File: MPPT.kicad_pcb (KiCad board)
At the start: 2 copper layers, 172.7 x 116.8 mm, 127 parts, among them J1 Solar Array, J2 Battery, J3 Car Power, J4 CAN_In, J5 CAN_Out, Q1 NMOS, Q2 NMOS, SW1 RESET, SW2 CAN Address, U1 PQMC3-D12-S9-S, U2 Nucleo_L432KC, U3 UCC37321, U4 INA210, U5 ADM3055E, U6 INA210, U7 CDSOT23-T24CAN, U8 MAX400_option2, U9 MAX400_option2

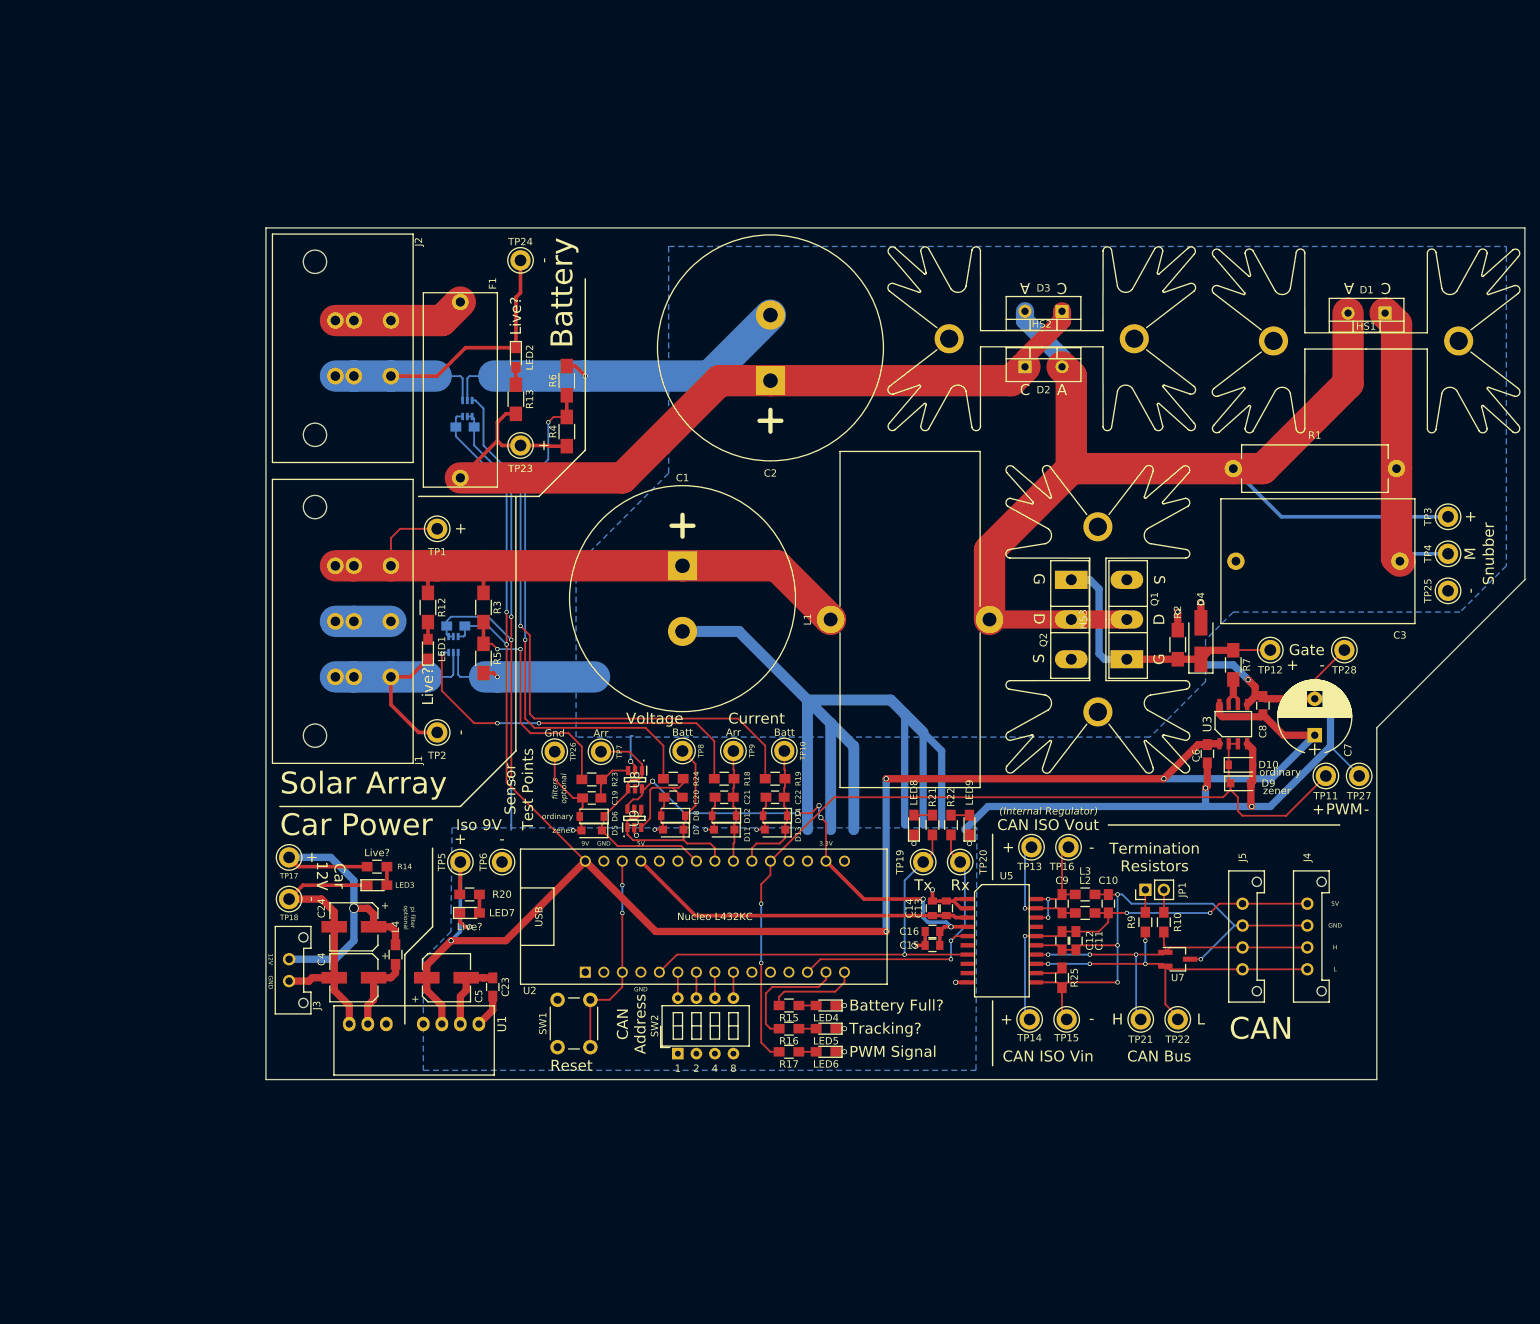
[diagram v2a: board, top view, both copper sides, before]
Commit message: Major MPPT Board update. Overhaul of layout, and cleanup of the schematic. Added further documentation and updated instructions in the README. Added unity gain op amp for voltage sensors.
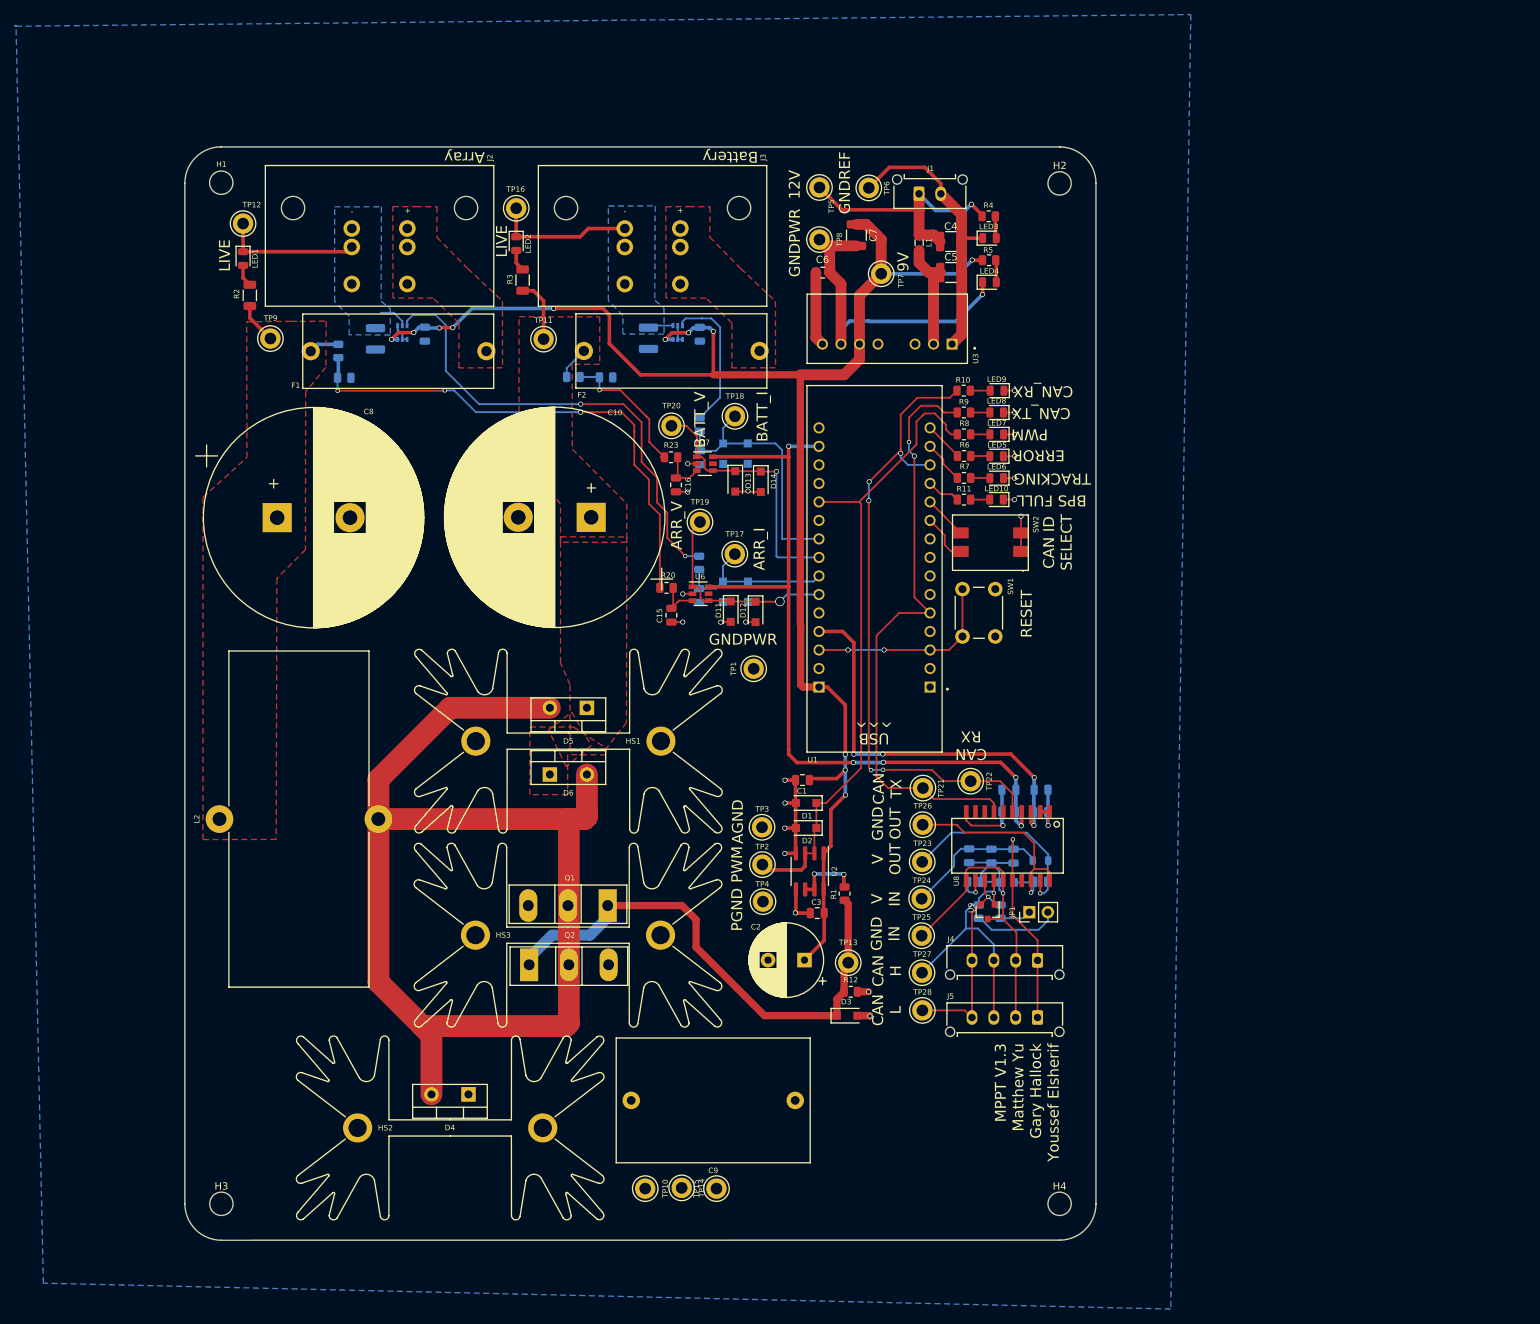
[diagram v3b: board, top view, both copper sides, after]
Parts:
- removed R13: 40K, Resistors_SMD:R_1206_HandSoldering
- added F2: Fuse, MPPT-PrimaryPCB:05200101Z_Fuze_Holder_5x20_PCB_Mount, F.Cu at (99.8, 53.1)
- added H1: Top Left Mounting Hole, MountingHole:MountingHole_3.2mm_M3, F.Cu at (25.0, 25.0)
- added H2: Top Right Mounting Hole, MountingHole:MountingHole_3.2mm_M3, F.Cu at (140.0, 25.0)
- added H3: Bottom Left Mounting Hole, MountingHole:MountingHole_3.2mm_M3, F.Cu at (25.0, 165.0)
- added H4: Bottom Right Mounting Hole, MountingHole:MountingHole_3.2mm_M3, F.Cu at (140.0, 165.0)
- added LED10: BPS Full (Blue), LED_SMD:LED_0805_2012Metric, F.Cu at (131.3, 68.4)
- added R26: 60, Resistor_SMD:R_0805_2012Metric, B.Cu at (131.9, 124.9)
- C1: value 1000uF -> 0.1uF; footprint UTSVT_Passive:CP_Radial_D31mm_P9mm -> Capacitor_SMD:C_0805_2012Metric
- C10: value 0.22u -> 1000uF; footprint Capacitors_SMD:C_0805_HandSoldering -> Capacitor_THT:CP_Radial_D30.0mm_P10.00mm_SnapIn
- C11: value 0.1u -> 0.1uF; footprint Capacitors_SMD:C_0805_HandSoldering -> Capacitor_SMD:C_0805_2012Metric; moved to B.Cu
- C12: value 0.01u -> 1uF; footprint Capacitors_SMD:C_0805_HandSoldering -> Capacitor_SMD:C_0805_2012Metric; moved to B.Cu
- C13: value 10u -> 0.1uF; footprint Capacitors_SMD:C_0805 -> Capacitor_SMD:C_0805_2012Metric; moved to B.Cu
- C14: value 0.1u -> 1uF; footprint Capacitors_SMD:C_0805 -> Capacitor_SMD:C_0805_2012Metric; moved to B.Cu
- C15: value 0.1u -> 1uF; footprint Capacitors_SMD:C_0805 -> Capacitor_SMD:C_0805_2012Metric
- C16: value 0.01u -> 1uF; footprint Capacitors_SMD:C_0805 -> Capacitor_SMD:C_0805_2012Metric
- C17: value 0.1uF -> 10uF; footprint Capacitors_SMD:C_0805_HandSoldering -> Capacitor_SMD:C_0805_2012Metric
- C18: footprint Capacitors_SMD:C_0805_HandSoldering -> Capacitor_SMD:C_0805_2012Metric
- C19: value 1uF -> 0.1uF; footprint Capacitors_SMD:C_0805_HandSoldering -> Capacitor_SMD:C_0805_2012Metric; moved to B.Cu
- C2: value 1000uF -> 1uF; footprint UTSVT_Passive:CP_Radial_D31mm_P9mm -> Capacitor_THT:CP_Radial_D10.0mm_P5.00mm
- C20: value 1uF -> 0.01uF; footprint Capacitors_SMD:C_0805_HandSoldering -> Capacitor_SMD:C_0805_2012Metric; moved to B.Cu
- C21: value 1uF -> 0.22uF; footprint Capacitors_SMD:C_0805_HandSoldering -> Capacitor_SMD:C_0805_2012Metric; moved to B.Cu
- C22: value 1uF -> 10uF; footprint Capacitors_SMD:C_0805_HandSoldering -> Capacitor_SMD:C_0805_2012Metric; moved to B.Cu
- C23: value 10u -> 0.01uF; footprint Capacitors_SMD:C_0805_HandSoldering -> Capacitor_SMD:C_0805_2012Metric; moved to B.Cu
- C24: value 100u -> 0.1uF; footprint Capacitors_SMD:CP_Elec_6.3x7.7 -> Capacitor_SMD:C_0805_2012Metric; moved to B.Cu
- C3: value CP -> 0.1uF; footprint MPPT_Custom:C_Rect_L26.5mm_W17.0mm_P22.50mm_MKS4 -> Capacitor_SMD:C_0805_2012Metric
- C4: value 47u -> 100uF; footprint Capacitors_SMD:CP_Elec_6.3x5.3 -> Capacitor_SMD:C_1210_3225Metric
- C5: value 100u -> 47uF; footprint Capacitors_SMD:CP_Elec_6.3x7.7 -> Capacitor_SMD:C_1210_3225Metric
- C6: value 0.1u -> 10uF; footprint Capacitors_SMD:C_0805_HandSoldering -> Capacitor_SMD:C_0805_2012Metric
- C7: value 1u -> 100uF; footprint Capacitors_THT:CP_Radial_D10.0mm_P5.00mm -> Capacitor_SMD:C_1210_3225Metric
- C8: value 0.1u -> 1000uF; footprint Capacitors_SMD:C_0805_HandSoldering -> Capacitor_THT:CP_Radial_D30.0mm_P10.00mm_SnapIn
- C9: value 10u -> CP; footprint Capacitors_SMD:C_0805_HandSoldering -> MPPT_Custom:C_Rect_L26.5mm_W17.0mm_P22.50mm_MKS4
- D1: value Schottky -> 3.9V Zener; footprint TO_SOT_Packages_THT:TO-220-2_Vertical -> Diode_SMD:D_SOD-123F
- D10, D8: footprint Diodes_SMD:D_SOD-123 -> Diode_SMD:D_SOD-123F; moved to B.Cu
- D11, D13: value 4V Zener -> 3.9V Zener; footprint Diodes_SMD:D_SOD-123F -> Diode_SMD:D_SOD-123F
- D12, D14: footprint Diodes_SMD:D_SOD-123 -> Diode_SMD:D_SOD-123F
- D2: value Schottky -> Diode; footprint TO_SOT_Packages_THT:TO-220-2_Vertical -> Diode_SMD:D_SOD-123F
- D3: value Schottky -> 16.3V Zener; footprint TO_SOT_Packages_THT:TO-220-2_Vertical -> Diode_SMD:D_SOD-123F
- D4: value 18V Zener -> Schottky; footprint Diodes_SMD:D_SMA_Handsoldering -> Package_TO_SOT_THT:TO-220-2_Vertical
- D5: value 4V Zener -> Schottky; footprint Diodes_SMD:D_SOD-123F -> Package_TO_SOT_THT:TO-220-2_Vertical
- D6: value Diode -> Schottky; footprint Diodes_SMD:D_SOD-123 -> Package_TO_SOT_THT:TO-220-2_Vertical
- D7, D9: value 4V Zener -> 3.9V Zener; footprint Diodes_SMD:D_SOD-123F -> Diode_SMD:D_SOD-123F; moved to B.Cu
- F1: footprint UTSVT_Passive:LittelFuse_OMNIBLOK_520Series_PCB -> MPPT-PrimaryPCB:05200101Z_Fuze_Holder_5x20_PCB_Mount
- HS1: value Heatsink -> Schottky Diode Heatsink
- HS2: value Heatsink -> Snubber Heatsink
- HS3: value Heatsink -> MOSFET Heatsink
- J1: value Solar Array -> Car Power; footprint UTSVT_Connectors:PhoenixContact_PowerCombicon5_GF_3x7.62mm -> Connector_Molex:Molex_Micro-Fit_3.0_43650-0215_1x02_P3.00mm_Vertical
- J2: value Battery -> Solar Array; footprint UTSVT_Connectors:PhoenixContact_PowerCombicon5_GF_2x7.62mm -> MPPT-PrimaryPCB:PhoenixContact_PowerCombicon5_GF_2x7.62mm
- J3: value Car Power -> Battery; footprint UTSVT_Connectors:Molex_MicroFit3.0_1x2xP3.00mm_PolarizingPeg_Vertical -> MPPT-PrimaryPCB:PhoenixContact_PowerCombicon5_GF_2x7.62mm
- J4, J5: footprint UTSVT_Connectors:Molex_MicroFit3.0_1x4xP3.00mm_PolarizingPeg_Vertical -> Connector_Molex:Molex_Micro-Fit_3.0_43650-0415_1x04_P3.00mm_Vertical
- JP1: footprint Pin_Headers:Pin_Header_Straight_1x02_Pitch2.54mm -> Connector_PinHeader_2.54mm:PinHeader_1x02_P2.54mm_Vertical
- L1: value 560uH -> 4.7uH; footprint Inductors_THT:L_Toroid_Vertical_L46.0mm_W19.1mm_P21.80mm_Bourns_5700 -> Inductor_SMD:L_0805_2012Metric
- L2: value 2k -> 560uH; footprint Inductors_SMD:L_0805_HandSoldering -> MPPT-PrimaryPCB:L_Toroid_Vertical_L46.0mm_W19.1mm_P21.80mm_Bourns_5700
- L3: value 2k -> 1.8kH; footprint Inductors_SMD:L_0805_HandSoldering -> Inductor_SMD:L_0805_2012Metric; moved to B.Cu
- L4: value 4.7u -> 1.8kH; footprint Inductors_SMD:L_0805_HandSoldering -> Inductor_SMD:L_0805_2012Metric; moved to B.Cu
- LED1: value Array Live? -> Array Live (Green); footprint LEDs:LED_0805_HandSoldering -> LED_SMD:LED_0805_2012Metric
- LED2: value Battery Live? -> Battery Live (Green); footprint LEDs:LED_0805_HandSoldering -> LED_SMD:LED_0805_2012Metric
- LED3: value Car Power Live? -> Car Power Live (Green); footprint LEDs:LED_0805_HandSoldering -> LED_SMD:LED_0805_2012Metric
- LED4: value Battery Full? -> Device 9V Live (Green); footprint LEDs:LED_0805_HandSoldering -> LED_SMD:LED_0805_2012Metric
- LED5: value Tracking? -> Error (Amber); footprint LEDs:LED_0805_HandSoldering -> LED_SMD:LED_0805_2012Metric
- LED6: value PWM -> Tracking (Blue); footprint LEDs:LED_0805_HandSoldering -> LED_SMD:LED_0805_2012Metric
- LED7: value Iso 9V Live? -> PWM (Blue); footprint LEDs:LED_0805_HandSoldering -> LED_SMD:LED_0805_2012Metric
- LED8: value CAN_Tx -> CAN_Tx (Blue); footprint LEDs:LED_0805_HandSoldering -> LED_SMD:LED_0805_2012Metric
- LED9: value CAN_Rx -> CAN_Rx (Blue); footprint LEDs:LED_0805_HandSoldering -> LED_SMD:LED_0805_2012Metric
- Q1, Q2: footprint TO_SOT_Packages_THT:TO-247_TO-3P_Vertical -> Package_TO_SOT_THT:TO-247-3_Vertical
- R1: value R -> 1.5; footprint Resistors_THT:R_Axial_Power_L20.0mm_W6.4mm_P22.40mm -> Resistor_SMD:R_0805_2012Metric
- R10, R9: value 60 -> 330; footprint Resistors_SMD:R_0805_HandSoldering -> Resistor_SMD:R_0805_2012Metric
- R11, R8: value 2m -> 330; footprint Resistors_SMD:R_2512_HandSoldering -> Resistor_SMD:R_0805_2012Metric; moved to F.Cu
- R12: value 40K -> 10k; footprint Resistors_SMD:R_1206_HandSoldering -> Resistor_SMD:R_0805_2012Metric
- R14: value 2K -> 2m; footprint Resistors_SMD:R_0805_HandSoldering -> Resistor_SMD:R_1210_3225Metric; moved to B.Cu
- R15, R17: value 330R -> 1.7k; footprint Resistors_SMD:R_0805_HandSoldering -> Resistor_SMD:R_0805_2012Metric; moved to B.Cu
- R16: value 330R -> 2m; footprint Resistors_SMD:R_0805_HandSoldering -> Resistor_SMD:R_1210_3225Metric; moved to B.Cu
- R18: value 1.7k -> 100k; footprint Resistors_SMD:R_0805_HandSoldering -> Resistor_SMD:R_0805_2012Metric; moved to B.Cu
- R19: value 1.7k -> 2k; footprint Resistors_SMD:R_0805_HandSoldering -> Resistor_SMD:R_0805_2012Metric; moved to B.Cu
- R2: value 10k -> 15k; footprint Resistors_SMD:R_1206_HandSoldering -> Resistor_SMD:R_1206_3216Metric
- R20: value 1K -> 1.7k; footprint Resistors_SMD:R_0805_HandSoldering -> Resistor_SMD:R_0805_2012Metric
- R21: value 330R -> 100k; footprint Resistors_SMD:R_0805_HandSoldering -> Resistor_SMD:R_0805_2012Metric; moved to B.Cu
- R22: value 330R -> 2k; footprint Resistors_SMD:R_0805_HandSoldering -> Resistor_SMD:R_0805_2012Metric; moved to B.Cu
- R23: footprint Resistors_SMD:R_0805_HandSoldering -> Resistor_SMD:R_0805_2012Metric
- R24: value 1.7k -> 0; footprint Resistors_SMD:R_0805_HandSoldering -> Resistor_SMD:R_0805_2012Metric; moved to B.Cu
- R25: value 0 -> 60; footprint Resistors_SMD:R_0805_HandSoldering -> Resistor_SMD:R_0805_2012Metric; moved to B.Cu
- R3: value 100k -> 27k; footprint Resistors_SMD:R_1206_HandSoldering -> Resistor_SMD:R_1206_3216Metric
- R4: value 100k -> 1.5k; footprint Resistors_SMD:R_1206_HandSoldering -> Resistor_SMD:R_0805_2012Metric
- R5: value 2k -> 1.1k; footprint Resistors_SMD:R_1206_HandSoldering -> Resistor_SMD:R_0805_2012Metric
- R6: value 2k -> 330; footprint Resistors_SMD:R_1206_HandSoldering -> Resistor_SMD:R_0805_2012Metric
- R7: value 1R5 -> 330; footprint Resistors_SMD:R_1206_HandSoldering -> Resistor_SMD:R_0805_2012Metric
- SW1: footprint Buttons_Switches_THT:SW_PUSH_6mm -> Button_Switch_THT:SW_PUSH_6mm
- SW2: value CAN Address -> SW_DIP_x02; footprint Buttons_Switches_THT:SW_DIP_x4_W7.62mm_Slide_LowProfile -> MPPT-PrimaryPCB:ADF02ST04_DIP_Switch_2_POS
- TP1: value +ARR -> GND; footprint Measurement_Points:Test_Point_Keystone_5005-5009_Compact -> TestPoint:TestPoint_Keystone_5005-5009_Compact
- TP10: value Batt_I -> +SNUB; footprint Measurement_Points:Test_Point_Keystone_5005-5009_Compact -> TestPoint:TestPoint_Keystone_5005-5009_Compact
- TP11: value PWM -> +BATT; footprint Measurement_Points:Test_Point_Keystone_5005-5009_Compact -> TestPoint:TestPoint_Keystone_5005-5009_Compact
- TP12: value GATE -> -ARR; footprint Measurement_Points:Test_Point_Keystone_5005-5009_Compact -> TestPoint:TestPoint_Keystone_5005-5009_Compact
- TP13: value CAN_ISO_Vout -> GATE; footprint Measurement_Points:Test_Point_Keystone_5005-5009_Compact -> TestPoint:TestPoint_Keystone_5005-5009_Compact
- TP14: value CAN_ISO_Vin -> M_SNUB; footprint Measurement_Points:Test_Point_Keystone_5005-5009_Compact -> TestPoint:TestPoint_Keystone_5005-5009_Compact
- TP15: value CAN_ISO_GndIn -> -SNUB; footprint Measurement_Points:Test_Point_Keystone_5005-5009_Compact -> TestPoint:TestPoint_Keystone_5005-5009_Compact
- TP16: value CAN_ISO_GndOut -> -BATT; footprint Measurement_Points:Test_Point_Keystone_5005-5009_Compact -> TestPoint:TestPoint_Keystone_5005-5009_Compact
- TP17: value Car +12V -> Arr_I; footprint Measurement_Points:Test_Point_Keystone_5005-5009_Compact -> TestPoint:TestPoint_Keystone_5005-5009_Compact
- TP18: value Car GND -> Batt_I; footprint Measurement_Points:Test_Point_Keystone_5005-5009_Compact -> TestPoint:TestPoint_Keystone_5005-5009_Compact
- TP19: value CAN_Tx -> Arr_V; footprint Measurement_Points:Test_Point_Keystone_5005-5009_Compact -> TestPoint:TestPoint_Keystone_5005-5009_Compact
- TP2: value -ARR -> PWM; footprint Measurement_Points:Test_Point_Keystone_5005-5009_Compact -> TestPoint:TestPoint_Keystone_5005-5009_Compact
- TP20: value CAN_Rx -> Batt_V; footprint Measurement_Points:Test_Point_Keystone_5005-5009_Compact -> TestPoint:TestPoint_Keystone_5005-5009_Compact
- TP21: value CAN_H -> CAN_Tx; footprint Measurement_Points:Test_Point_Keystone_5005-5009_Compact -> TestPoint:TestPoint_Keystone_5005-5009_Compact
- TP22: value CAN_L -> CAN_Rx; footprint Measurement_Points:Test_Point_Keystone_5005-5009_Compact -> TestPoint:TestPoint_Keystone_5005-5009_Compact
- TP23: value +BATT -> CAN_ISO_Vout; footprint Measurement_Points:Test_Point_Keystone_5005-5009_Compact -> TestPoint:TestPoint_Keystone_5005-5009_Compact
- TP24: value -BATT -> CAN_ISO_Vin; footprint Measurement_Points:Test_Point_Keystone_5005-5009_Compact -> TestPoint:TestPoint_Keystone_5005-5009_Compact
- TP25: value -SNUB -> CAN_ISO_GndIn; footprint Measurement_Points:Test_Point_Keystone_5005-5009_Compact -> TestPoint:TestPoint_Keystone_5005-5009_Compact
- TP26: value GND -> CAN_ISO_GndOut; footprint Measurement_Points:Test_Point_Keystone_5005-5009_Compact -> TestPoint:TestPoint_Keystone_5005-5009_Compact
- TP27: value AGND -> CAN_H; footprint Measurement_Points:Test_Point_Keystone_5005-5009_Compact -> TestPoint:TestPoint_Keystone_5005-5009_Compact
- TP28: value PGND -> CAN_L; footprint Measurement_Points:Test_Point_Keystone_5005-5009_Compact -> TestPoint:TestPoint_Keystone_5005-5009_Compact
- TP3: value +SNUB -> AGND; footprint Measurement_Points:Test_Point_Keystone_5005-5009_Compact -> TestPoint:TestPoint_Keystone_5005-5009_Compact
- TP4: value M_SNUB -> PGND; footprint Measurement_Points:Test_Point_Keystone_5005-5009_Compact -> TestPoint:TestPoint_Keystone_5005-5009_Compact
- TP5: value +9VA -> Car +12V; footprint Measurement_Points:Test_Point_Keystone_5005-5009_Compact -> TestPoint:TestPoint_Keystone_5005-5009_Compact
- TP6: value GNDP -> Car GND; footprint Measurement_Points:Test_Point_Keystone_5005-5009_Compact -> TestPoint:TestPoint_Keystone_5005-5009_Compact
- TP7: value Arr_V -> +9VA; footprint Measurement_Points:Test_Point_Keystone_5005-5009_Compact -> TestPoint:TestPoint_Keystone_5005-5009_Compact
- TP8: value Batt_V -> GNDP; footprint Measurement_Points:Test_Point_Keystone_5005-5009_Compact -> TestPoint:TestPoint_Keystone_5005-5009_Compact
- TP9: value Arr_I -> +ARR; footprint Measurement_Points:Test_Point_Keystone_5005-5009_Compact -> TestPoint:TestPoint_Keystone_5005-5009_Compact
- U1: value PQMC3-D12-S9-S -> Nucleo_L432KC; footprint UTSVT_ICs:CUI_PQMC3-S -> MPPT-PrimaryPCB:MODULE_NUCLEO-L432KC
- U2: value Nucleo_L432KC -> UCC37321; footprint UTSVT_Special:NucleoL432KC -> Package_SO:SOIC-8_3.9x4.9mm_P1.27mm
- U3: value UCC37321 -> PQMC3-D12-S9-S; footprint UTSVT_ICs:SOIC-8_4.00x5.00mm_Pitch1.27mm -> MPPT-PrimaryPCB:490_PQMC3_D12_S12_S
- U4: footprint UTSVT_ICs:SOIC-6_1.40x2.15mm_Pitch0.65mm -> MPPT-PrimaryPCB:SC70-6
- U5: value ADM3055E -> INA210; footprint UTSVT_ICs:SOIC-20W_7.5x15.4mm_Pitch1.27mm -> MPPT-PrimaryPCB:SC70-6; moved to B.Cu
- U6: value INA210 -> MAX40075AUT+; footprint UTSVT_ICs:SOIC-6_1.40x2.15mm_Pitch0.65mm -> Package_TO_SOT_SMD:SOT-23-6; moved to F.Cu
- U7: value CDSOT23-T24CAN -> MAX40075AUT+; footprint TO_SOT_Packages_SMD:SOT-23W_Handsoldering -> Package_TO_SOT_SMD:SOT-23-6
- U8: value MAX400_option2 -> ADM3055E; footprint MPPT_Custom:SOT95P280X145-6N -> MPPT-PrimaryPCB:ADM3055EBRIZ
- U9: value MAX400_option2 -> CDSOT23-T24CAN; footprint MPPT_Custom:SOT95P280X145-6N -> Package_TO_SOT_SMD:SOT-23
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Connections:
- C1 pad 1: /+Arr -> GNDPWR
- C1 pad 2: GNDPWR -> +9VA
- C10 pad 1: Net-(C10-Pad1) -> /+Batt
- C10 pad 2: Net-(C10-Pad2) -> GNDPWR
- C11 pad 1: Net-(C10-Pad1) -> +9VA
- C11 pad 2: Net-(C10-Pad2) -> GNDPWR
- C12 pad 1: Net-(C10-Pad1) -> /Array_Current
- C12 pad 2: Net-(C10-Pad2) -> GNDPWR
- C13 pad 1: +5V -> +9VA
- C14 pad 1: +5V -> /Battery_Current
- C15 pad 1: +3V3 -> Net-(C15-Pad1)
- C16 pad 1: +3V3 -> Net-(C16-Pad1)
- C17 pad 1: +9VA -> +5V
- C18 pad 1: +9VA -> +5V
- C19 pad 1: Net-(C19-Pad1) -> +3V3
- C2 pad 1: /+Batt -> +9VA
- C20 pad 1: Net-(C20-Pad1) -> +3V3
- C21 pad 1: /Array_Current -> Net-(C21-Pad1)
- C21 pad 2: GNDPWR -> Net-(C21-Pad2)
- C22 pad 1: /Battery_Current -> Net-(C22-Pad1)
- C22 pad 2: GNDPWR -> Net-(C22-Pad2)
- C23 pad 1: GNDPWR -> Net-(C22-Pad1)
- C23 pad 2: Net-(C23-Pad2) -> Net-(C22-Pad2)
- C24 pad 1: +12V -> Net-(C22-Pad1)
- C24 pad 2: GNDREF -> Net-(C22-Pad2)
- C3 pad 1: Net-(C3-Pad1) -> +9VA
- C4 pad 1: Net-(C4-Pad1) -> +12V
- C5 pad 1: +9VA -> Net-(C5-Pad1)
- C5 pad 2: GNDPWR -> GNDREF
- C6 pad 2: +9VA -> Net-(C6-Pad2)
- C8 pad 1: +9VA -> /+Arr
- C9 pad 2: Net-(C9-Pad2) -> GNDPWR
- D1 pad 1: Net-(C3-Pad1) -> /PWM
- D1 pad 2: Net-(D1-Pad2) -> GNDPWR
- D10 pad 1: /PWM -> /Battery_Current
- D11 pad 1: /Array_Current -> /Array_Voltage
- D12 pad 1: /Array_Current -> /Array_Voltage
- D13 pad 1: /Battery_Current -> /Battery_Voltage
- D14 pad 1: /Battery_Current -> /Battery_Voltage
- D2 pad 1: /+Batt -> /PWM
- D2 pad 2: Net-(D1-Pad2) -> GNDPWR
- D3 pad 1: /+Batt -> /Drive_PWM
- D3 pad 2: Net-(D1-Pad2) -> GNDPWR
- D4 pad 1: /Drive_PWM -> Net-(C9-Pad1)
- D4 pad 2: GNDPWR -> Net-(D4-Pad2)
- D5 pad 1: /Array_Voltage -> /+Batt
- D5 pad 2: GNDPWR -> Net-(D4-Pad2)
- D6 pad 1: /Array_Voltage -> /+Batt
- D6 pad 2: GNDPWR -> Net-(D4-Pad2)
- D7 pad 1: /Battery_Voltage -> /Array_Current
- D8 pad 1: /Battery_Voltage -> /Array_Current
- D9 pad 1: /PWM -> /Battery_Current
- F1 pad 2: /+Batt -> /+Arr
- J1 pad 1: /+Arr -> +12V
- J1 pad 2: Net-(J1-Pad2) -> GNDREF
- J2 pad 2: /-Batt -> /-Arr
- J3 pad 1: +12V -> Net-(F2-Pad1)
- J3 pad 2: GNDREF -> /-Batt
- J4 pad 1: Net-(C10-Pad1) -> Net-(C22-Pad1)
- J4 pad 2: Net-(C10-Pad2) -> Net-(C22-Pad2)
- J5 pad 1: Net-(C10-Pad1) -> Net-(C22-Pad1)
- J5 pad 2: Net-(C10-Pad2) -> Net-(C22-Pad2)
- L1 pad 1: /+Arr -> +12V
- L1 pad 2: Net-(D1-Pad2) -> Net-(C5-Pad1)
- L2 pad 1: Net-(C10-Pad1) -> /+Arr
- L2 pad 2: Net-(C9-Pad1) -> Net-(D4-Pad2)
- L3 pad 1: Net-(C10-Pad2) -> Net-(C22-Pad1)
- L3 pad 2: Net-(C9-Pad2) -> Net-(C21-Pad1)
- L4 pad 1: +12V -> Net-(C22-Pad2)
- L4 pad 2: Net-(C4-Pad1) -> Net-(C21-Pad2)
- Q1 pad 2: Net-(D1-Pad2) -> Net-(D4-Pad2)
- Q2 pad 2: Net-(D1-Pad2) -> Net-(D4-Pad2)
- R1 pad 1: Net-(D1-Pad2) -> /Drive_PWM
- R1 pad 2: Net-(C3-Pad1) -> Net-(R1-Pad2)
- R10 pad 1: Net-(JP1-Pad2) -> Net-(LED9-Pad2)
- R10 pad 2: Net-(J4-Pad3) -> /CAN_Rx
- R11 pad 1: /-Batt -> Net-(LED10-Pad2)
- R11 pad 2: GNDPWR -> /BPS_Full
- R12 pad 1: Net-(LED1-Pad2) -> /Drive_PWM
- R12 pad 2: /+Arr -> GNDPWR
- R14 pad 1: Net-(LED3-Pad2) -> GNDPWR
- R14 pad 2: +12V -> /-Arr
- R15 pad 1: Net-(LED4-Pad2) -> Net-(R15-Pad1)
- R15 pad 2: /Battery_Full -> /Array_Current
- R16 pad 1: Net-(LED5-Pad2) -> /-Batt
- R16 pad 2: /Tracking -> GNDPWR
- R17 pad 1: Net-(LED6-Pad2) -> Net-(R17-Pad1)
- R17 pad 2: /PWM -> /Battery_Current
- R18 pad 1: Net-(R18-Pad1) -> /+Arr
- R18 pad 2: /Array_Current -> Net-(R18-Pad2)
- R19 pad 1: Net-(R19-Pad1) -> Net-(R18-Pad2)
- R19 pad 2: /Battery_Current -> GNDPWR
- R2 pad 1: /Drive_PWM -> Net-(LED1-Pad2)
- R2 pad 2: GNDPWR -> /+Arr
- R20 pad 1: Net-(LED7-Pad2) -> Net-(R18-Pad2)
- R20 pad 2: +9VA -> Net-(C15-Pad1)
- R21 pad 1: Net-(LED8-Pad2) -> /+Batt
- R21 pad 2: /CAN_Tx -> Net-(R21-Pad2)
- R22 pad 1: Net-(LED9-Pad2) -> Net-(R21-Pad2)
- R22 pad 2: /CAN_Rx -> GNDPWR
- R23 pad 1: Net-(R23-Pad1) -> Net-(R21-Pad2)
- R23 pad 2: Net-(C19-Pad1) -> Net-(C16-Pad1)
- R24 pad 2: Net-(C20-Pad1) -> Net-(C22-Pad2)
- R25 pad 1: Net-(R25-Pad1) -> Net-(JP1-Pad2)
- R25 pad 2: Net-(C10-Pad2) -> Net-(J4-Pad3)
- R3 pad 1: /+Arr -> Net-(LED2-Pad2)
- R3 pad 2: Net-(R23-Pad1) -> /+Batt
- R4 pad 1: /+Batt -> Net-(LED3-Pad2)
- R4 pad 2: Net-(R24-Pad1) -> +12V
- R5 pad 1: Net-(R23-Pad1) -> Net-(LED4-Pad2)
- R5 pad 2: GNDPWR -> +9VA
- R6 pad 1: Net-(R24-Pad1) -> Net-(LED5-Pad2)
- R6 pad 2: GNDPWR -> /Error
- R7 pad 1: /Drive_PWM -> Net-(LED6-Pad2)
- R7 pad 2: Net-(R7-Pad2) -> /Tracking
- R8 pad 1: GNDPWR -> Net-(LED7-Pad2)
- R8 pad 2: /-Arr -> /PWM
- R9 pad 1: Net-(JP1-Pad1) -> Net-(LED8-Pad2)
- R9 pad 2: Net-(J4-Pad4) -> /CAN_Tx
- SW1 pad 1: GNDPWR -> /Reset
- SW1 pad 2: /Reset -> GNDPWR
- SW2 pad 3: GNDPWR -> Net-(SW2-Pad3)
- SW2 pad 4: GNDPWR -> Net-(SW2-Pad4)
- TP1 pad 1: /+Arr -> GNDPWR
- TP10 pad 1: /Battery_Current -> Net-(D4-Pad2)
- TP11 pad 1: /PWM -> /+Batt
- TP12 pad 1: /Drive_PWM -> /-Arr
- TP13 pad 1: Net-(C9-Pad1) -> /Drive_PWM
- TP14 pad 1: Net-(C10-Pad1) -> Net-(C9-Pad1)
- TP15 pad 1: Net-(C10-Pad2) -> GNDPWR
- TP16 pad 1: Net-(C9-Pad2) -> /-Batt
- TP17 pad 1: +12V -> /Array_Current
- TP18 pad 1: GNDREF -> /Battery_Current
- TP19 pad 1: /CAN_Tx -> /Array_Voltage
- TP2 pad 1: /-Arr -> /PWM
- TP20 pad 1: /CAN_Rx -> /Battery_Voltage
- TP21 pad 1: Net-(J4-Pad3) -> /CAN_Tx
- TP22 pad 1: Net-(J4-Pad4) -> /CAN_Rx
- TP23 pad 1: /+Batt -> Net-(C21-Pad1)
- TP24 pad 1: /-Batt -> Net-(C22-Pad1)
- TP25 pad 1: GNDPWR -> Net-(C22-Pad2)
- TP26 pad 1: GNDPWR -> Net-(C21-Pad2)
- TP27 pad 1: GNDPWR -> Net-(J4-Pad3)
- TP28 pad 1: GNDPWR -> Net-(J4-Pad4)
- TP3 pad 1: Net-(D1-Pad2) -> GNDPWR
- TP4 pad 1: Net-(C3-Pad1) -> GNDPWR
- TP5 pad 1: +9VA -> +12V
- TP6 pad 1: GNDPWR -> GNDREF
- TP7 pad 1: /Array_Voltage -> +9VA
- TP8 pad 1: /Battery_Voltage -> GNDPWR
- TP9 pad 1: /Array_Current -> /+Arr
- U1 pad 1: GNDREF -> Net-(U1-Pad1)
- U1 pad 2: Net-(C4-Pad1) -> Net-(U1-Pad2)
- U1 pad 3: Net-(U1-Pad3) -> /Reset
- U1 pad 5: Net-(U1-Pad5) -> /CAN_Tx
- U1 pad 6: +9VA -> Net-(U1-Pad6)
- U1 pad 7: GNDPWR -> Net-(U1-Pad7)
- U1 pad 8: Net-(C23-Pad2) -> Net-(U1-Pad8)
- U2 pad 1: Net-(U2-Pad1) -> +9VA
- U2 pad 2: Net-(U2-Pad2) -> /PWM
- U2 pad 3: /Reset -> /PWM
- U2 pad 5: /CAN_Tx -> GNDPWR
- U2 pad 6: Net-(SW2-Pad8) -> Net-(R1-Pad2)
- U2 pad 7: Net-(SW2-Pad7) -> Net-(R1-Pad2)
- U2 pad 8: Net-(SW2-Pad6) -> +9VA
- U3 pad 1: +9VA -> GNDREF
- U3 pad 2: /PWM -> Net-(C5-Pad1)
- U3 pad 3: /PWM -> Net-(U3-Pad3)
- U3 pad 5: GNDPWR -> Net-(U3-Pad5)
- U3 pad 6: Net-(R7-Pad2) -> +9VA
- U3 pad 7: Net-(R7-Pad2) -> GNDPWR
- U3 pad 8: +9VA -> Net-(C6-Pad2)
- U4 pad 6: Net-(R18-Pad1) -> Net-(R15-Pad1)
- U5 pad 3: +5V -> +9VA
- U5 pad 4: +3V3 -> /-Batt
- U5 pad 5: /CAN_Rx -> GNDPWR
- U5 pad 6: Net-(U5-Pad6) -> Net-(R17-Pad1)
- U6 pad 1: GNDPWR -> /Array_Voltage
- U6 pad 3: +9VA -> Net-(C15-Pad1)
- U6 pad 4: /-Batt -> /Array_Voltage
- U6 pad 5: GNDPWR -> Net-(U6-Pad5)
- U6 pad 6: Net-(R19-Pad1) -> +3V3
- U7 pad 1: Net-(J4-Pad3) -> /Battery_Voltage
- U7 pad 2: Net-(J4-Pad4) -> GNDPWR
- U7 pad 3: Net-(C10-Pad2) -> Net-(C16-Pad1)
- U8 pad 1: /Array_Voltage -> GNDPWR
- U8 pad 3: Net-(C19-Pad1) -> +5V
- U8 pad 4: /Array_Voltage -> +3V3
- U8 pad 5: Net-(U8-Pad5) -> /CAN_Rx
- U8 pad 6: +3V3 -> Net-(U8-Pad6)
- U9 pad 1: /Battery_Voltage -> Net-(J4-Pad3)
- U9 pad 2: GNDPWR -> Net-(J4-Pad4)
- U9 pad 3: Net-(C20-Pad1) -> Net-(C22-Pad2)
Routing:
- net GNDPWR: track 470.7 -> 122.3 mm, vias 25 -> 24
- net Net-(D4-Pad2): track 0.00 -> 156.7 mm
- net Net-(D1-Pad2): track 153.1 -> 0.00 mm
- net /+Batt: track 116.1 -> 13.3 mm
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- added copper zone on F.Cu, net /+Arr
- added copper zone on F.Cu, net /+Batt
- added copper zone on B.Cu, net /-Arr
- added copper zone on B.Cu, net /-Batt
- added copper zone on F.Cu, net Net-(F1-Pad1)
- added copper zone on F.Cu, net Net-(F2-Pad1)
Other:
- board size 172.7 x 116.8 mm -> 125 x 150 mm
- board text added: "AGND"
- board text added: "ARR_I"
- board text added: "ARR_V"
- board text added: "Array"
- board text added: "BATT_I"
- board text added: "BATT_V"
- board text added: "BPS FULL"
- board text added: "CAN H"
- board text added: "CAN ID SELECT"
- board text added: "CAN L"
- board text added: "CAN RX"
- board text added: "CAN TX"
- board text added: "CAN_RX"
- board text added: "CAN_TX"
- board text added: "ERROR"
- board text added: "GND IN"
- board text added: "GND OUT"
- board text added: "GNDPWR"
- board text added: "GNDREF"
- board text added: "I am concerned about routing thin analog signals across two power planes for high power systems. Especially where the MPPT is attempting to shift the voltage to maximize the current, sometimes in large steps."
- board text added: "I could've just used B.Cu for CAN_TX and CAN_RX since GNDPWR isn't in the way, but I was unsure how much crosstalk the digital signal might get."
- board text added: "I don't like how this 9V line runs across multiple high power planes. Route from top?"
- board text added: "I have concern about overlapping these sensor circuits.."
- board text added: "I wonder if this voltage out of the divider is too close.."
- board text added: "LIVE"
- board text added: "Leave some space for metadata. Component sections should also have identifying labels. All chips or polarized components should be marked for positive/pin1."
- board text added: "MPPT V1.3 Matthew Yu Gary Hallock Youssef Elsherif"
- board text added: "Need to figure out what the possible snubber values could be and select a generic footprint to fit them."
- board text added: "PGND"
- board text added: "RESET"
- board text added: "Should check again what the tolerances and padding should be around these components in the heatsink."
- board text added: "Star ground separating digital logic from analog."
- board text added: "TRACKING"
- board text added: "U4"
- board text added: "U5"
- board text added: "USB ^^^"
- board text added: "Unused"
- board text added: "V IN"
- board text added: "V OUT"
- board text added: "We can probably cut the layout down another 3-5% if we use smaller, more efficient heat sinks."
- board text added: "uC might want to be moved over a little bit more and the 9V line expanded to 2mm and 1mm lines to CAN and Drive PWM."
- board text removed: "(Internal Regulator)"
- board text removed: "."
- board text removed: "1"
- board text removed: "2"
- board text removed: "3.3V"
- board text removed: "4"
- board text removed: "5V"
- board text removed: "8"
- board text removed: "A"
- board text removed: "Arr"
- board text removed: "Batt"
- board text removed: "Battery Full?"
- board text removed: "C"
- board text removed: "CAN"
- board text removed: "CAN Address"
- board text removed: "CAN Bus"
- board text removed: "CAN ISO Vin"
- board text removed: "CAN ISO Vout"
- board text removed: "Car 12V"
- board text removed: "Car Power"
- board text removed: "Current"
- board text removed: "D"
- board text removed: "G"
- board text removed: "GND"
- board text removed: "Gate"
- board text removed: "Gnd"
- board text removed: "H"
- board text removed: "Iso 9V"
- board text removed: "L"
- board text removed: "Live?"
- board text removed: "M"
- board text removed: "NC"
- board text removed: "Optional: Ground Heat Sink be careful about isolation!"
- board text removed: "PWM Signal"
- board text removed: "Reset"
- board text removed: "Rx"
- board text removed: "S"
- board text removed: "Sensor Test Points"
- board text removed: "Snubber"
- board text removed: "Solar Array"
- board text removed: "Termination Resistors"
- board text removed: "Tracking?"
- board text removed: "Tx"
- board text removed: "Voltage"
- board text removed: "filters optional"
- board text removed: "ordinary"
- board text removed: "pi filter optional"
- board text removed: "zener"

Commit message: Finalized board layout.
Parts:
- added G***: LOGO, UTSVT_Special:UTSVT_Logo_Symbol, B.Cu at (35.8, 27.7)
- added G***: LOGO, UTSVT_Special:Hallock_Image_Tiny, F.Cu at (49.5, 31.0)
- added R13: R, Package_TO_SOT_THT:TO-220-2_Vertical, F.Cu at (104.6, 47.1)
- C2: footprint Capacitor_THT:CP_Radial_D10.0mm_P5.00mm -> Capacitor_SMD:C_0805_2012Metric; moved to B.Cu
- C9: footprint MPPT_Custom:C_Rect_L26.5mm_W17.0mm_P22.50mm_MKS4 -> Capacitor_THT:C_Rect_L16.5mm_W7.0mm_P15.00mm_MKT
- D1, D2, R12: moved to B.Cu
- TP8: value GNDP -> Device GND
- moved H4 184.7 mm to (22.5, 22.5), turned to 180 degrees
- moved H3 181.6 mm to (137.5, 22.5), turned to 180 degrees
- moved H2 177.1 mm to (22.5, 157.5), turned to 180 degrees
- moved H1 173.8 mm to (137.5, 157.5), turned to 180 degrees
- moved TP12 161.6 mm to (134.5, 152.0), turned to 0 degrees
- moved R4 157.6 mm to (32.2, 153.0), turned to 0 degrees
- moved LED1 154.5 mm to (134.5, 147.2), turned to 90 degrees
- moved LED3 153.1 mm to (32.1, 150.0), turned to 180 degrees
- moved J1 151.7 mm to (41.8, 156.0), turned to 180 degrees
- moved J5 148.6 mm to (23.8, 43.0), turned to 0 degrees
- moved R5 148.5 mm to (32.2, 146.9), turned to 0 degrees
- moved R2 146.6 mm to (134.4, 142.1), turned to 90 degrees
- moved TP6 146.5 mm to (48.7, 156.8), turned to 90 degrees
- moved C4 145.8 mm to (37.4, 149.5), turned to 180 degrees
- moved LED4 144.0 mm to (32.1, 143.9), turned to 180 degrees
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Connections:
- C1 pad 1: GNDPWR -> GNDREF
- C10 pad 2: GNDPWR -> GNDREF
- C11 pad 2: GNDPWR -> GNDREF
- C12 pad 2: GNDPWR -> GNDREF
- C13 pad 2: GNDPWR -> GNDREF
- C14 pad 2: GNDPWR -> GNDREF
- C15 pad 2: GNDPWR -> GNDREF
- C16 pad 2: GNDPWR -> GNDREF
- C17 pad 2: GNDPWR -> GNDREF
- C18 pad 2: GNDPWR -> GNDREF
- C19 pad 2: GNDPWR -> GNDREF
- C2 pad 2: GNDPWR -> GNDREF
- C20 pad 2: GNDPWR -> GNDREF
- C3 pad 2: GNDPWR -> GNDREF
- C4 pad 2: GNDREF -> GNDPWR
- C5 pad 2: GNDREF -> GNDPWR
- C6 pad 1: GNDPWR -> GNDREF
- C7 pad 2: GNDPWR -> GNDREF
- C8 pad 2: GNDPWR -> GNDREF
- C9 pad 2: GNDPWR -> GNDREF
- D1 pad 2: GNDPWR -> GNDREF
- D10 pad 2: GNDPWR -> GNDREF
- D11 pad 2: GNDPWR -> GNDREF
- D12 pad 2: GNDPWR -> GNDREF
- D13 pad 2: GNDPWR -> GNDREF
- D14 pad 2: GNDPWR -> GNDREF
- D2 pad 2: GNDPWR -> GNDREF
- D3 pad 2: GNDPWR -> GNDREF
- D7 pad 2: GNDPWR -> GNDREF
- D8 pad 2: GNDPWR -> GNDREF
- D9 pad 2: GNDPWR -> GNDREF
- J1 pad 2: GNDREF -> GNDPWR
- LED10 pad 1: GNDPWR -> GNDREF
- LED3 pad 1: GNDREF -> GNDPWR
- LED4 pad 1: GNDPWR -> GNDREF
- LED5 pad 1: GNDPWR -> GNDREF
- LED6 pad 1: GNDPWR -> GNDREF
- LED7 pad 1: GNDPWR -> GNDREF
- LED8 pad 1: GNDPWR -> GNDREF
- LED9 pad 1: GNDPWR -> GNDREF
- Q1 pad 3: GNDPWR -> GNDREF
- Q2 pad 3: GNDPWR -> GNDREF
- R12 pad 2: GNDPWR -> GNDREF
- R14 pad 1: GNDPWR -> GNDREF
- R16 pad 2: GNDPWR -> GNDREF
- R19 pad 2: GNDPWR -> GNDREF
- R22 pad 2: GNDPWR -> GNDREF
- SW1 pad 2: GNDPWR -> GNDREF
- SW2 pad 1: GNDPWR -> GNDREF
- SW2 pad 2: GNDPWR -> GNDREF
- TP1 pad 1: GNDPWR -> GNDREF
- TP15 pad 1: GNDPWR -> GNDREF
- TP3 pad 1: GNDPWR -> GNDREF
- TP4 pad 1: GNDPWR -> GNDREF
- TP6 pad 1: GNDREF -> GNDPWR
- TP8 pad 1: GNDPWR -> GNDREF
- U1 pad 29: GNDPWR -> GNDREF
- U1 pad 4: GNDPWR -> GNDREF
- U2 pad 4: GNDPWR -> GNDREF
- U2 pad 5: GNDPWR -> GNDREF
- U3 pad 1: GNDREF -> GNDPWR
- U3 pad 7: GNDPWR -> GNDREF
- U4 pad 1: GNDPWR -> GNDREF
- U4 pad 2: GNDPWR -> GNDREF
- U4 pad 4: GNDPWR -> GNDREF
- U5 pad 1: GNDPWR -> GNDREF
- U5 pad 2: GNDPWR -> GNDREF
- U5 pad 5: GNDPWR -> GNDREF
- U6 pad 2: GNDPWR -> GNDREF
- U7 pad 2: GNDPWR -> GNDREF
- U8 pad 1: GNDPWR -> GNDREF
- U8 pad 10: GNDPWR -> GNDREF
- U8 pad 2: GNDPWR -> GNDREF
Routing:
- net GNDREF: track 38.8 -> 126.5 mm, vias 0 -> 22
- net GNDPWR: track 122.3 -> 38.8 mm, vias 24 -> 0
- net Net-(C9-Pad1): track 0.00 -> 35.7 mm
- net +9VA: track 218.0 -> 204.9 mm
- net /Drive_PWM: track 73.0 -> 61.2 mm, vias 0 -> 1
- net /PWM: track 88.6 -> 82.1 mm, vias 0 -> 2
- net Net-(D4-Pad2): track 156.7 -> 153.9 mm
- net /CAN_Tx: track 82.5 -> 84.2 mm
- net /CAN_Rx: track 88.6 -> 90.3 mm
- net +5V: track 55.5 -> 57.2 mm
- net +3V3: track 109.4 -> 111.1 mm
- net /+Batt: track 13.3 -> 14.0 mm
- added copper zone on B.Cu, net GNDREF
- removed copper zone on B.Cu, net GNDPWR
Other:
- board size 125 x 150 mm -> 125 x 145 mm
- board text added: "+12V"
- board text added: "+9VA"
- board text added: "ARR LIVE"
- board text added: "ARR+"
- board text added: "BATT LIVE"
- board text added: "BATT+"
- board text added: "Board GND"
- board text added: "CAN Circuit"
- board text added: "CANH"
- board text added: "CANL"
- board text added: "Car GND"
- board text added: "Car PWR"
- board text added: "GNDIN"
- board text added: "Gate"
- board text added: "In principle, I am concerned about routing thin analog signals across two power planes for high power systems. Especially in the case where the system is attempting to rapidly shift the voltage to maximize the current, sometimes in large steps, which may cause outsized current fluctuations and electromagnetic interference."
- board text added: "UTSVT - Array MPPT v1.3 Fall 2020 Youssef Elsherif Gary Hallock Matthew Yu"
- board text added: "VIN"
- board text added: "VOUT"
- board text removed: "12V"
- board text removed: "9V"
- board text removed: "CAN H"
- board text removed: "CAN L"
- board text removed: "GND IN"
- board text removed: "GNDPWR"
- board text removed: "I am concerned about routing thin analog signals across two power planes for high power systems. Especially where the MPPT is attempting to shift the voltage to maximize the current, sometimes in large steps."
- board text removed: "I don't like how this 9V line runs across multiple high power planes. Route from top?"
- board text removed: "I have concern about overlapping these sensor circuits.."
- board text removed: "I wonder if this voltage out of the divider is too close.."
- board text removed: "LIVE"
- board text removed: "Leave some space for metadata. Component sections should also have identifying labels. All chips or polarized components should be marked for positive/pin1."
- board text removed: "MPPT V1.3 Matthew Yu Gary Hallock Youssef Elsherif"
- board text removed: "Need to figure out what the possible snubber values could be and select a generic footprint to fit them."
- board text removed: "Should check again what the tolerances and padding should be around these components in the heatsink."
- board text removed: "V IN"
- board text removed: "V OUT"
- board text removed: "We can probably cut the layout down another 3-5% if we use smaller, more efficient heat sinks."
- board text removed: "uC might want to be moved over a little bit more and the 9V line expanded to 2mm and 1mm lines to CAN and Drive PWM."
